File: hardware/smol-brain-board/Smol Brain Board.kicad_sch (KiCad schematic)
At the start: 71 parts, among them J1 USB4085-GF-A, J10 Jumper 2Way Vert Solderable, J11 Jumper Solderable, J2 Jumper Solderable, J3 CAN_DBG, J4 Jumper 2Way Vert Solderable, J5 Jumper 2Way Vert Solderable, J6 Smol_Brain_Board, J7 PROGRAM, J8 Jumper 2Way Vert Solderable, J9 Jumper 2Way Vert Solderable, U1 ESP32-S3-WROOM-1-N8, U2 AP63203WU-7, U3 SN65HVD232D

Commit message: Fixing schematic of Smol brain board
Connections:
- net A2: now also R5.1, U1.37 (TXD0)
- net IO15: now also R17.2, U1.10 (IO17)
- net UART0_RX: now also R7.1, U1.36 (RXD0)
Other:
- moved on the sheet: C11, C7, C8, CAN_RX1, CAN_TX1, CRX1, CTX1, D3, D5, J10, J3, R12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

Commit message: Updating footprints and symbols
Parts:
- removed C13: Capacitor 4.7n 50V 0603, FP-CC0603-DA-IPC_B, symbol QUTRC ARC:root_1_11868f565c42a9108669ba33697ecf6_QUTRC ARC
- removed J11: Jumper Solderable, Jumper_2Way_Solderable, symbol QUTRC ARC:root_2_CMP-015-000006-1_QUTRC ARC
- removed J2: Jumper Solderable, Jumper 2Way Side Solderable-Footprint-1, symbol QUTRC ARC:root_2_CMP-015-000006-1_QUTRC ARC
- removed R20, R21: 62R 0.25W 1206, RESC3216X60X45LL10T20, symbol Altium Content Vault:root_1_RES_Altium Content Vault_0
- removed R4: Resistor 5.1k 0603, FP-RMCF0603-IPC_A, symbol QUTRC ARC:root_0_1029c3af85768c4190bb7ad29bc67b5_QUTRC ARC
- added J12: Jumper 2Way Vert Solderable, Jumper:SolderJumper-2_P1.3mm_Open_TrianglePad1.0x1.5mm, symbol Jumper:SolderJumper_2_Open
- added R4: Resistor 5.1k 0603, Resistor_SMD:R_0201_0603Metric, symbol Device:R
- 3V3, CAN_TX1, VBUS1: footprint Testpoint_1x2mm -> TestPoint:TestPoint_Pad_D2.0mm; symbol QUTRC ARC:root_1_Testpoint_QUTRC ARC -> Connector:TestPoint
- 3V3_IND1, VIN_IND1: footprint LTST-C191KRKT_V -> LED_SMD:LED_0603_1608Metric; symbol QUTRC ARC:root_3_LED-RED-AK-2_QUTRC ARC -> Device:LED
- AP63203WU-7: renamed from U2; footprint FP-TSOT26-MFG -> Package_TO_SOT_SMD:TSOT-23-6; symbol Altium Content Vault:root_0_0e61c2974d7114b43f01ef96ae2e524_Altium Content Vault -> Regulator_Switching:AP63203WU
- BOOT1, RST1: footprint FP-PTS636_SKG25_SMTR_LFS-MFG -> Button_Switch_SMD:SW_MEC_5GSH9; symbol Altium Content Vault:root_0_bdfe703aeb3461bf7c331fe9d798369_Altium Content Vault -> Switch:SW_Push
- C1, C10, C11, C2, C3, C7, C8, C9: symbol QUTRC ARC:root_0_b4654b650e69147ec39a6b967a45e02_QUTRC ARC -> Device:C
- C12: symbol QUTRC ARC:root_1_b4654b650e69147ec39a6b967a45e02_QUTRC ARC -> Device:C
- C5, C6: symbol Altium Content Vault:root_0_b4654b650e69147ec39a6b967a45e02_Altium Content Vault -> Device:C
- CAN_RX1, GND1: footprint Testpoint_1x2mm -> TestPoint:TestPoint_Pad_D2.0mm; symbol QUTRC ARC:root_3_Testpoint_QUTRC ARC -> Connector:TestPoint
- CRX1: footprint LTST-C190GKT_V -> LED_SMD:LED_0603_1608Metric; symbol QUTRC ARC:root_1_LED-GREEN-AK-2_QUTRC ARC -> Device:LED
- CTX1: footprint LTST-C190KSKT_V -> LED_SMD:LED_0603_1608Metric; symbol QUTRC ARC:root_1_LED-YELLOW-AK-2_QUTRC ARC -> Device:LED
- D1, D4: footprint SODFL3618X110N -> Diode_SMD:D_SOD-323F; symbol QUTRC ARC:root_0_DSS14UTR_QUTRC ARC -> Device:D_Schottky
- D2: footprint FP-SMB-MFG -> Diode_SMD:D_SMA; symbol Altium Content Vault:root_1_7ddec9f632b8482e96f7745d0fbdf39_Altium Content Vault -> Diode:SMAJ6.5A
- D3: footprint FP-SOT-23-3L-MFG -> Package_TO_SOT_SMD:SOT-23; symbol Altium Content Vault:root_3_d1c11092ec5f108c7f6ec7cc86671a9_Altium Content Vault -> Device:D_TVS_Dual_CAA
- D5: footprint FP-SMBJ-MFG -> Diode_SMD:D_SMA; symbol Altium Content Vault:root_1_f813f71cba58e380607f5dd3caf9714_Altium Content Vault -> Diode:SMAJ26A
- D7: footprint INF-SOT323_M -> Package_TO_SOT_SMD:SOT-416; symbol QUTRC ARC:root_1_INF-D_A1K2C3-3_QUTRC ARC -> Diode:BAT54S; ADDITIONAL FEATURE HIGH RELIABILITY -> (none); DIODE ELEMENT MATERIAL SILICON -> (none); DIODE TYPE RECTIFIER -> (none); FORWARD CURRENT 100mA -> (none); FORWARD VOLTAGE 490mV -> (none); JESD-30 CODE R-PDSO-F3 -> (none); MAX OPERATING TEMPERATURE 125°C -> (none); MAX OUTPUT CURRENT 100mA -> (none); NUMBER OF ELEMENTS 2 -> (none); PACKAGE BODY MATERIAL Plastic -> (none); PACKAGE SHAPE Rectangular -> (none); PACKAGE STYLE SMALL OUTLINEMeter -> (none); PEAK INVERSE VOLTAGE 30V -> (none); PINS 3 -> (none); REACH SVHC COMPLIANT Yes -> (none); REP PK REVERSE VOLTAGE-MAX 30V -> (none); ROHS COMPLIANT Yes -> (none); SURFACE MOUNT Yes -> (none); TECHNOLOGY SCHOTTKY -> (none); TERMINAL FORM Flat -> (none); TERMINAL POSITION DUAL -> (none)
- F1: symbol QUTRC ARC:root_0_5bcf9b9f640e542cf0359d10258e979_QUTRC ARC -> Device:Fuse
- F2: symbol Altium Content Vault:root_0_5bcf9b9f640e542cf0359d10258e979_Altium Content Vault -> Device:Fuse
- J1: footprint FP-USB4085-GF-A-MFG -> Connector_USB:USB_C_Receptacle_GCT_USB4085; symbol Altium Content Vault:root_0_10fa745527c8b974685cbca3c197132_Altium Content Vault -> Connector:USB_C_Plug_USB2.0
- J10, J4, J5: footprint Jumper_2Way_Solderable -> Jumper:SolderJumper-2_P1.3mm_Open_TrianglePad1.0x1.5mm; symbol QUTRC ARC:root_0_CMP-015-000007-1_QUTRC ARC -> Jumper:SolderJumper_2_Open; now left out of the parts list
- J3: footprint PinHeader_1x03_P2.54mm_Vertical -> Connector_JST:JST_XH_B3B-XH-A_1x03_P2.50mm_Vertical; symbol QUTRC ARC:root_0_Conn_01x03_QUTRC ARC -> Connector_Generic:Conn_01x03
- J7: footprint PinHeader_1x05_P2.54mm_Vertical -> Connector_PinHeader_1.00mm:PinHeader_1x05_P1.00mm_Vertical; symbol QUTRC ARC:root_0_Conn_01x05_QUTRC ARC -> Connector_Generic:Conn_01x05
- J8, J9: footprint Jumper_2Way_Solderable -> Jumper:SolderJumper-2_P1.3mm_Open_TrianglePad1.0x1.5mm; symbol QUTRC ARC:root_1_CMP-015-000007-1_QUTRC ARC -> Jumper:SolderJumper_2_Open; now left out of the parts list
- L1: symbol QUTRC ARC:root_0_725321dda6339637d4d059423bc1c3c_QUTRC ARC -> Device:L
- R1, R12, R14, R16, R19, R3, R6: footprint FP-RMCF0603-IPC_A -> Resistor_SMD:R_0201_0603Metric; symbol QUTRC ARC:root_1_1029c3af85768c4190bb7ad29bc67b5_QUTRC ARC -> Device:R
- R10, R11, R13, R17, R18, R2, R5, R7: footprint FP-RMCF0603-IPC_A -> Resistor_SMD:R_0201_0603Metric; symbol QUTRC ARC:root_0_1029c3af85768c4190bb7ad29bc67b5_QUTRC ARC -> Device:R
- R15, R9: footprint FP-RMCF0603-IPC_A -> Resistor_SMD:R_0201_0603Metric; symbol QUTRC ARC:root_3_1029c3af85768c4190bb7ad29bc67b5_QUTRC ARC -> Device:R
- R8: footprint FP-RMCF0603-IPC_A -> Resistor_SMD:R_0201_0603Metric; symbol QUTRC ARC:root_2_1029c3af85768c4190bb7ad29bc67b5_QUTRC ARC -> Device:R
- STATUS1: footprint ADA-RGB-1655_V -> LED_SMD:LED_WS2812B_PLCC4_5.0x5.0mm_P3.2mm; symbol QUTRC ARC:root_0_ADA-RGB-1655-4_QUTRC ARC -> LED:WS2812B
- U1: footprint ESP32-S3-WROOM-1-N8_EXP -> RF_Module:ESP32-S3-WROOM-1; symbol QUTRC ARC:root_0_ESP32-S3-WROOM-1-N8_QUTRC ARC -> RF_Module:ESP32-S3-WROOM-1
- U3: value SN65HVD232D -> SN65HVD231D; footprint D0008A_L -> Package_SO:SOIC-8_3.9x4.9mm_P1.27mm; symbol Altium Content Vault:root_0_TI-SN65HVD232-SOIC_D-8_Altium Content Vault -> Interface_CAN_LIN:SN65HVD231
- VCC1: footprint Testpoint_1x2mm -> TestPoint:TestPoint_Pad_D2.0mm; symbol QUTRC ARC:root_0_Testpoint_QUTRC ARC -> Connector:TestPoint
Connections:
- net 3V3: now also 3V3_IND1.2 (A), CRX1.2 (A), CTX1.2 (A), R1.1, R19.1, R3.1, R6.1, R8.2, STATUS1.4 (DIN), J12.2 (B); no longer 3V3_IND1.1 (A), CRX1.1 (A), CTX1.1 (A), R1.2, R19.2, R3.2, R6.2
- net A2: no longer R5.1, U1.37 (TXD0)
- net CAN_H: now also D3.3 (A2); no longer D3.1
- net CAN_RX: now also R14.1; no longer R14.2
- net CAN_TX: now also R12.1, R19.2; no longer R12.2, R19.1
- net GND: now also D3.1 (common), J1.S1 (SHIELD), J10.1 (A), J5.1 (A), R16.2, R2.1, R4.2; no longer BOOT1.3 (GROUND), BOOT1.4 (GROUND), D3.3, J1.1 (MNT_1), J1.2 (MNT_2), J1.3 (MNT_3), J1.4 (MNT_4), J10.2, J5.2, R16.1, R2.2, RST1.3 (GROUND), RST1.4 (GROUND)
- net I2C_SCK: now also R1.2; no longer R1.1
- net I2C_SDA: now also R3.2; no longer R3.1
- net IO15: no longer R17.2, U1.10 (IO17)
- net RST: now also R6.2; no longer R6.1
- net UART0_RX: now also R5.1; no longer R7.1, R7.2, U1.36 (RXD0)
- net UART0_TX: now also R7.2; no longer R5.2
- net UART1_RX: now also R17.2; no longer R18.1
- net UART1_TX: now also R18.1; no longer R17.1
- net USB_D_N: now also D6.1 (1_CATHODE); no longer D6.2 (2_CATHODE), J1.B7 (Dn2)
- net USB_D_P: now also D6.2 (2_CATHODE); no longer D6.1 (1_CATHODE), J1.B6 (Dp2)
- net VBUS: now also D4.2 (A); no longer D4.A
- net VIN: now also D1.2 (A); no longer D1.A
- net uC_LED: now also R16.1, R8.1; no longer R16.2, R8.2
- net uC_USB_D_N: now also U1.14 (USB_D+); no longer U1.13 (IO19)
- net uC_USB_D_P: now also U1.13 (USB_D-); no longer U1.14 (IO20)
- net at AP63203WU-7.3 (IN), C4.1, F2.2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: now also F1.1, VIN_IND1.2 (A); no longer F1.2, VIN_IND1.1 (A)
- net at AP63203WU-7.5 (SW), L1.1: now also C3.1; no longer C3.2
- net at R9.1: now also VIN_IND1.1 (K); no longer VIN_IND1.2 (K)
- net at AP63203WU-7.2 (EN), J4.2 (B): now also J5.2 (B); no longer J5.1
- net at J1.A5 (CC): now also R4.1; no longer R2.1
- net at AP63203WU-7.6 (BST): now also C3.2; no longer C3.1
- net at R15.1: now also 3V3_IND1.1 (K); no longer 3V3_IND1.2 (K)
- net at J1.B5 (VCONN): now also R2.2
- net at F2.1: now also D4.1 (K); no longer D4.C (K)
- net at U3.8 (Rs): now also J10.2 (B), J12.1 (A); no longer J10.1
- new net: R17.1, U1.10 (IO17)
- new net: CRX1.1 (K), R14.2
- new net: R5.2, U1.36 (RXD0)
- new net: R7.1, U1.37 (TXD0)
- new net: D1.1 (K), D5.1 (A1), F1.2
- new net: CTX1.1 (K), R12.2
- no-connect marks 3 -> 1
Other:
- note added: "5.1k CC + VCONN to ground = 5V 3A supply"
- note added: "James Nichol, Brock Morgan"
- note removed: "${##}"
- note removed: "${#}"
- note removed: "${APPROVEDBY}"
- note removed: "${CURRENTTIME}"
- note removed: "${CURRENT_DATE}"
- note removed: "${ENGINEER}"
- note removed: "${PROJECT}"
- note removed: "${REVISION}"
- note removed: "${SUBSYSTEM}"
- note removed: "${TITLE}"
- note removed: "5.1k CC1 + CC2 to ground = 5V, 3A supply"
- note removed: "A3"
- note removed: "APPROVED"
- note removed: "DATE"
- note removed: "ENGINEER"
- note removed: "OF"
- note removed: "PROJECT"
- note removed: "REVISION"
- note removed: "SBU N/C"
- note removed: "SHEET"
- note removed: "SIZE"
- note removed: "SUBSYSTEM"
- note removed: "TITLE"
- moved on the sheet: 3V3, AP63203WU-7, C4, CAN_RX1, CAN_TX1, D6, GND1, J10, J3, J4, J5, J6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

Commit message: Starting footprint design
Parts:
- BOOT1, RST1: footprint Button_Switch_SMD:SW_MEC_5GSH9 -> Button_Switch_SMD:SW_SPST_CK_RS282G05A3
- C1: footprint FP-CL21-IPC_A -> Capacitor_SMD:C_0805_2012Metric
- C10, C11, C2, C3, C7, C8, C9: footprint FP-CL10-IPC_A -> Capacitor_SMD:C_0603_1608Metric
- C12: footprint FP-CL10-IPC_B -> Capacitor_SMD:C_0603_1608Metric
- C4: footprint FP-GRM188-0_2-IPC_A -> Capacitor_SMD:C_0603_1608Metric; symbol Altium Content Vault:root_0_11868f565c42a9108669ba33697ecf6_Altium Content Vault -> Device:C
- C5, C6: footprint FP-CL21-IPC_A -> Capacitor_SMD:C_0603_1608Metric
- D6: footprint FP-SOT23-3L-0053390-MFG -> Package_TO_SOT_SMD:SOT-416; symbol Altium Content Vault:root_3_852f986ac35c0497f1e372686d5e728_Altium Content Vault -> Power_Protection:RCLAMP0502B
- F1: footprint RESC4632X12N -> Fuse:Fuse_1812_4532Metric
- F2: footprint FP-SF-0603S-MFG -> Fuse:Fuse_0603_1608Metric
- J6: footprint Smol_Brain_Board_Male -> (none)
- L1: footprint FP-NR4018-MFG -> Inductor_SMD:L_Taiyo-Yuden_MD-4040
- renumbered AP63203WU-7 to VR1
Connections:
- net USB_D_N: now also D6.2 (K2); no longer D6.1 (1_CATHODE)
- net USB_D_P: now also D6.1 (K1); no longer D6.2 (2_CATHODE)

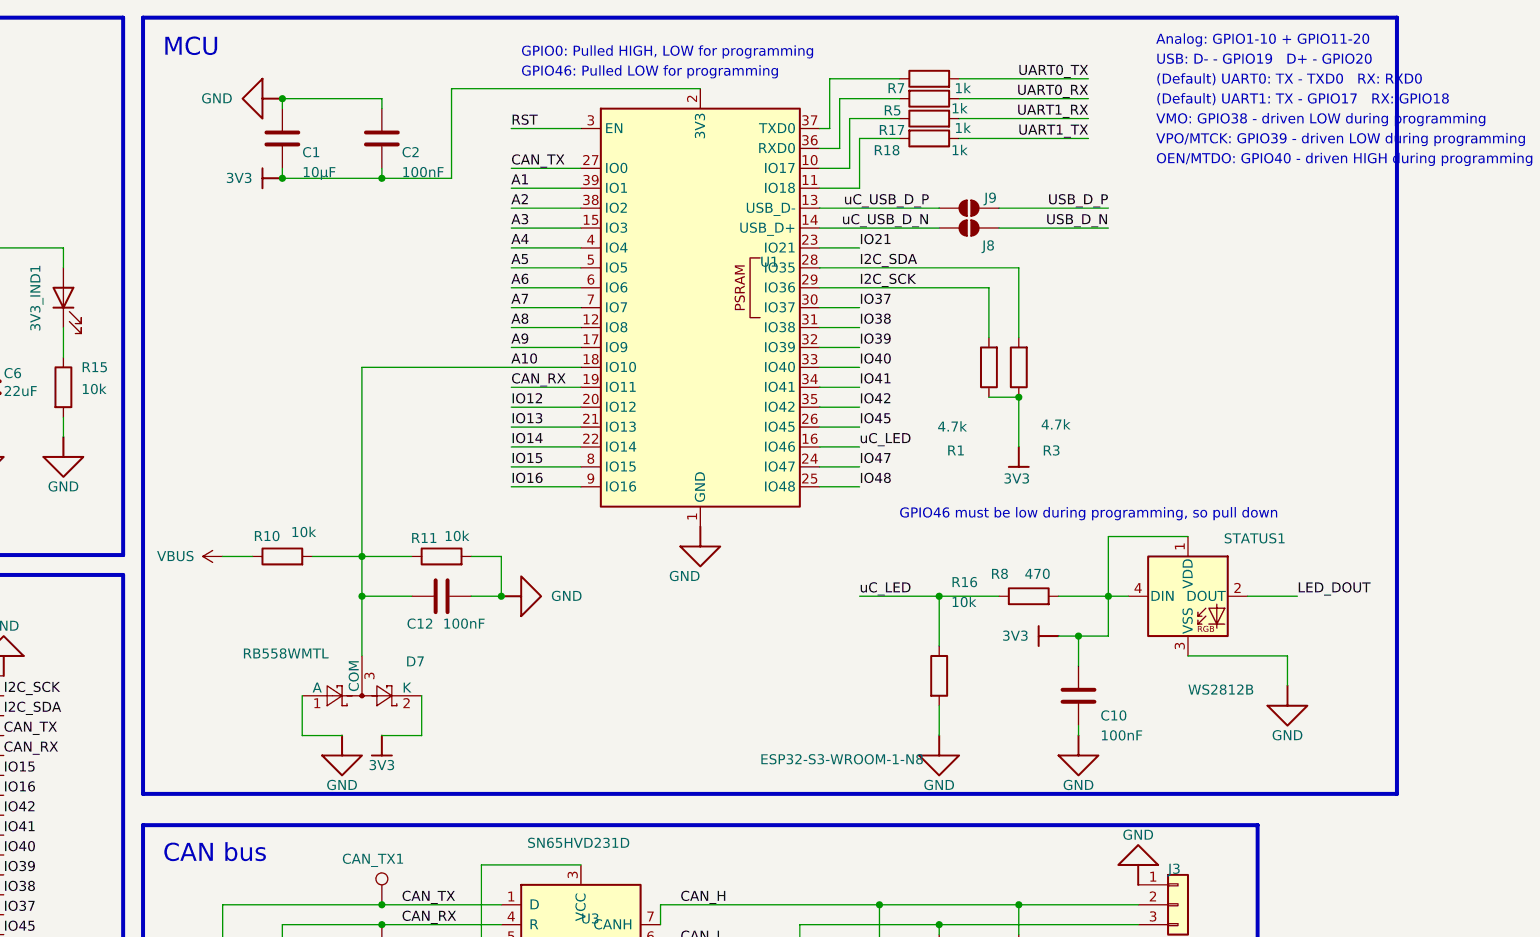
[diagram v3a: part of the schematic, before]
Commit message: Silkscreen labels and moving stuff around
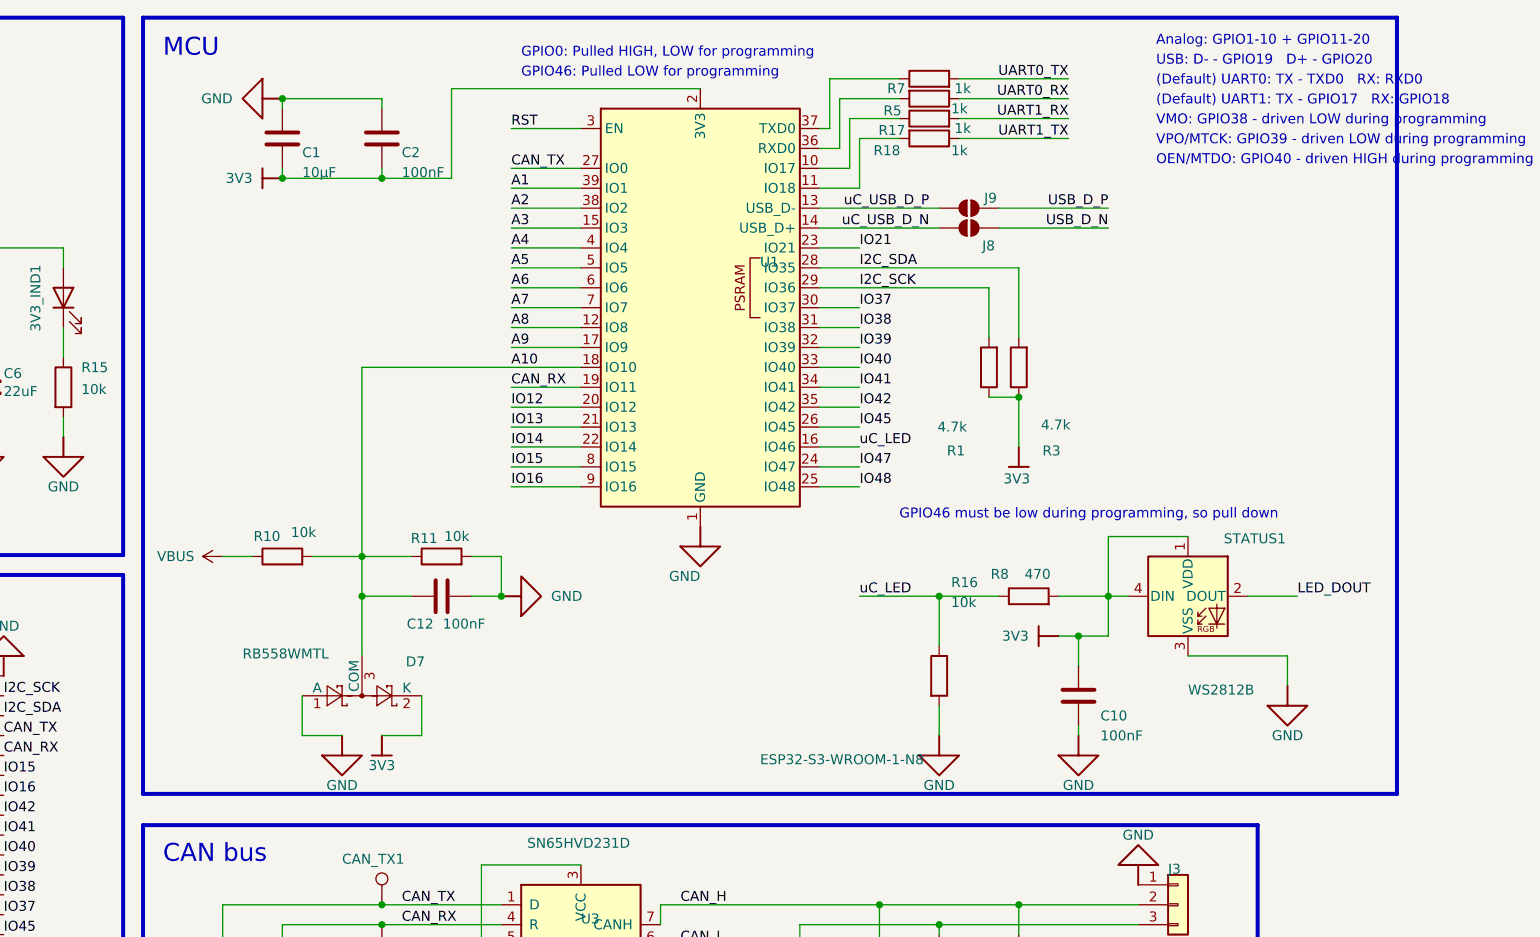
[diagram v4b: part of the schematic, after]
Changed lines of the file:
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@@
 	)
 	(rectangle
-		(start 396.24 21.4122)
-		(end 236.22 120.4722)
+		(start 236.22 21.4122)
+		(end 396.24 120.4722)
 		(stroke
 			(width 0.508)
@@
 	(wire
 		(pts
-			(xy 340.36 34.29) (xy 356.87 34.29)
+			(xy 340.36 34.29) (xy 354.33 34.29)
 		)
 		(stroke
@@
 	(wire
 		(pts
-			(xy 340.36 36.83) (xy 356.87 36.83)
+			(xy 340.36 36.83) (xy 354.33 36.83)
 		)
 		(stroke
@@
 	(wire
 		(pts
-			(xy 340.36 31.75) (xy 356.87 31.75)
+			(xy 340.36 31.75) (xy 354.33 31.75)
 		)
 		(stroke
@@
 	(wire
 		(pts
-			(xy 340.36 29.21) (xy 356.87 29.21)
+			(xy 340.36 29.21) (xy 354.33 29.21)
 		)
 		(stroke
@@
 	)
 	(label "UART1_TX"
-		(at 356.87 36.83 180)
+		(at 354.33 36.83 180)
 		(effects
 			(font
@@
 	)
 	(label "UART1_RX"
-		(at 356.87 34.29 180)
+		(at 354.33 34.29 180)
 		(effects
 			(font
@@
 		)
 	)
+	(label "UART1_TX"
+		(at 165.1 115.57 0)
+		(effects
+			(font
+				(size 1.27 1.27)
+			)
+			(justify left bottom)
+		)
+	)
 	(label "UART0_TX"
-		(at 356.87 29.21 180)
+		(at 354.33 29.21 180)
 		(effects
 			(font
@@
 		)
 	)
-	(label "UART1_TX"
-		(at 165.1 115.57 0)
-		(effects
-			(font
-				(size 1.27 1.27)
-			)
-			(justify left bottom)
-		)
-	)
 	(label "UART0_RX"
-		(at 356.87 31.75 180)
+		(at 354.33 31.75 180)
 		(effects
 			(font

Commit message: Start of routing
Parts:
- removed J10, J4: Jumper 2Way Vert Solderable, Jumper:SolderJumper-2_P1.3mm_Open_TrianglePad1.0x1.5mm, symbol Jumper:SolderJumper_2_Open
- added JP1, JP2: SolderJumper_2_Bridged, Jumper:SolderJumper-2_P1.3mm_Bridged_RoundedPad1.0x1.5mm, symbol Jumper:SolderJumper_2_Bridged
- J12, J8, J9: footprint Jumper:SolderJumper-2_P1.3mm_Open_TrianglePad1.0x1.5mm -> Jumper:SolderJumper-2_P1.3mm_Open_RoundedPad1.0x1.5mm
- J5: footprint Jumper:SolderJumper-2_P1.3mm_Open_TrianglePad1.0x1.5mm -> Jumper:SolderJumper-2_P1.3mm_Bridged_RoundedPad1.0x1.5mm
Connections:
- net GND: now also JP1.1 (A)
- net at C4.1, F1.1, F2.2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: now also JP2.2 (B)
- net at J5.2 (B), VR1.2 (EN): now also JP2.1 (A)
- net at J12.1 (A), U3.8 (Rs): now also JP1.2 (B)
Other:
- note added: "James Nichol, Brock Morgan, Maurice Blake"
- note removed: "James Nichol, Brock Morgan"
- moved on the sheet: 3V3, 3V3_IND1, BOOT1, C11, C3, C4, C5, C6, C7, C8, C9, CAN_RX1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
